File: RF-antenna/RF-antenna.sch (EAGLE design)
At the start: 7 parts, among them X1 SMA-V, X2 SMA-V, X3 SMA-V, X4 SMA-V, X5 SMA-V, X6 SMA-V

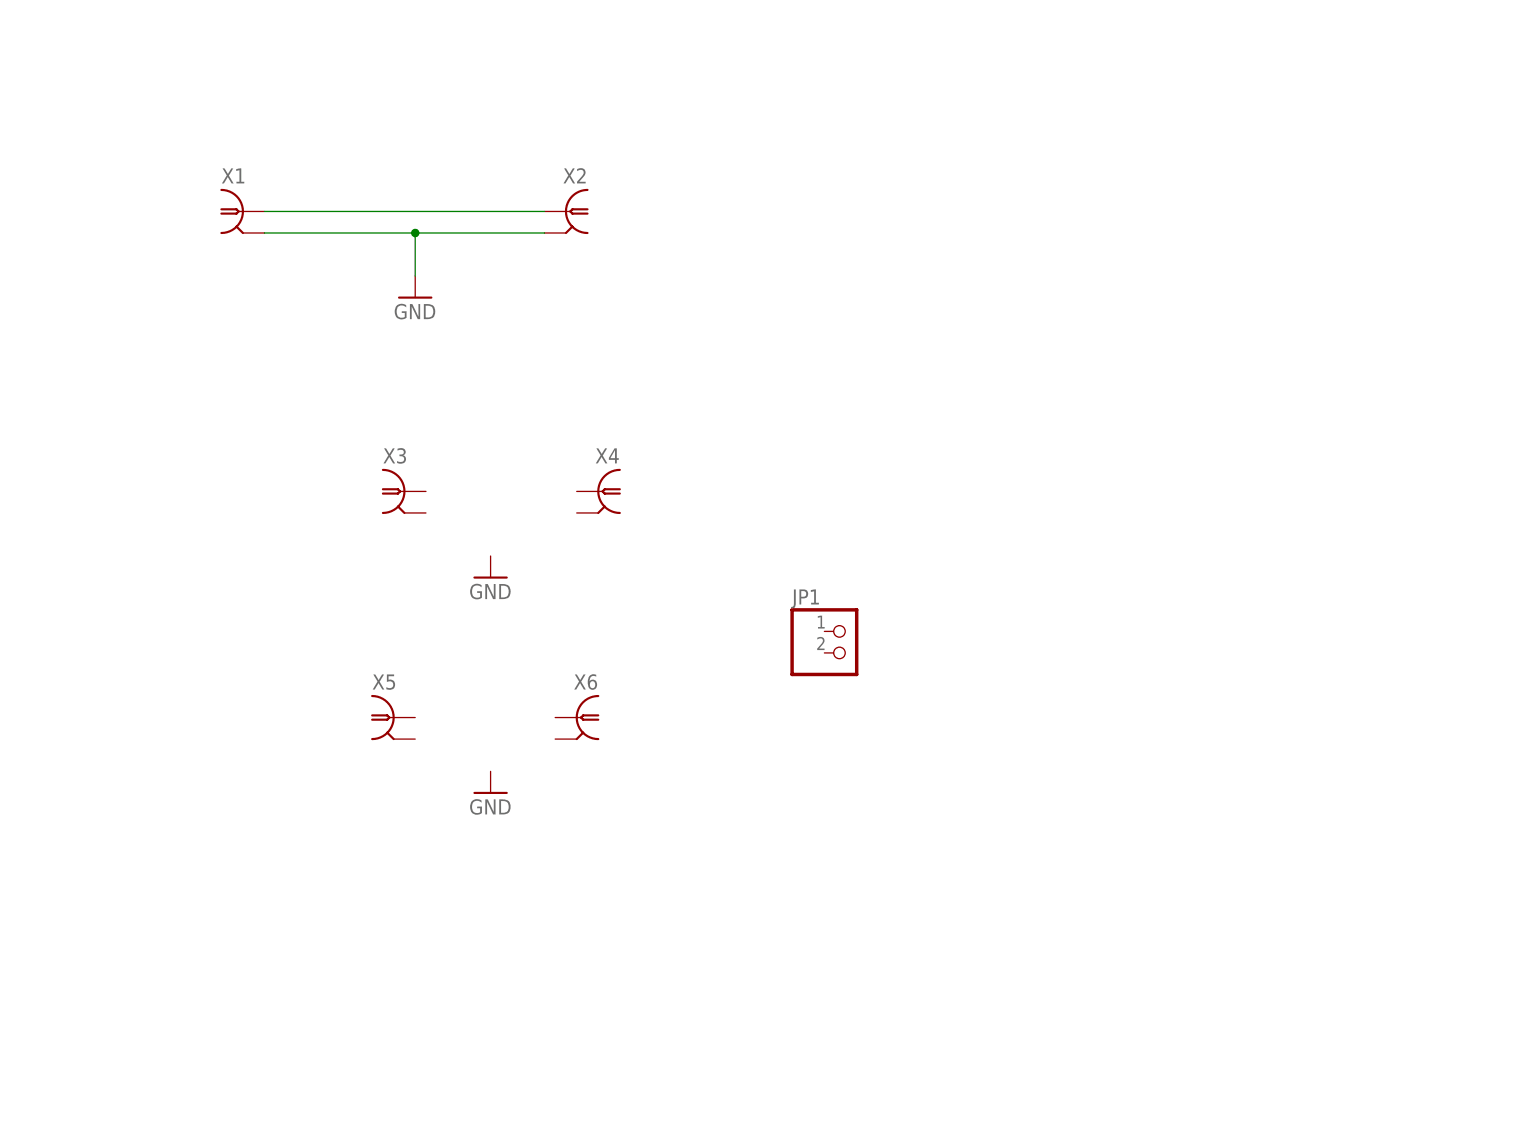
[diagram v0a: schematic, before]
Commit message: Adding parts for footprinting
Added a bunch of test components to get an idea of how tight the design
will be. Also corrected the keepout areas.

DSB
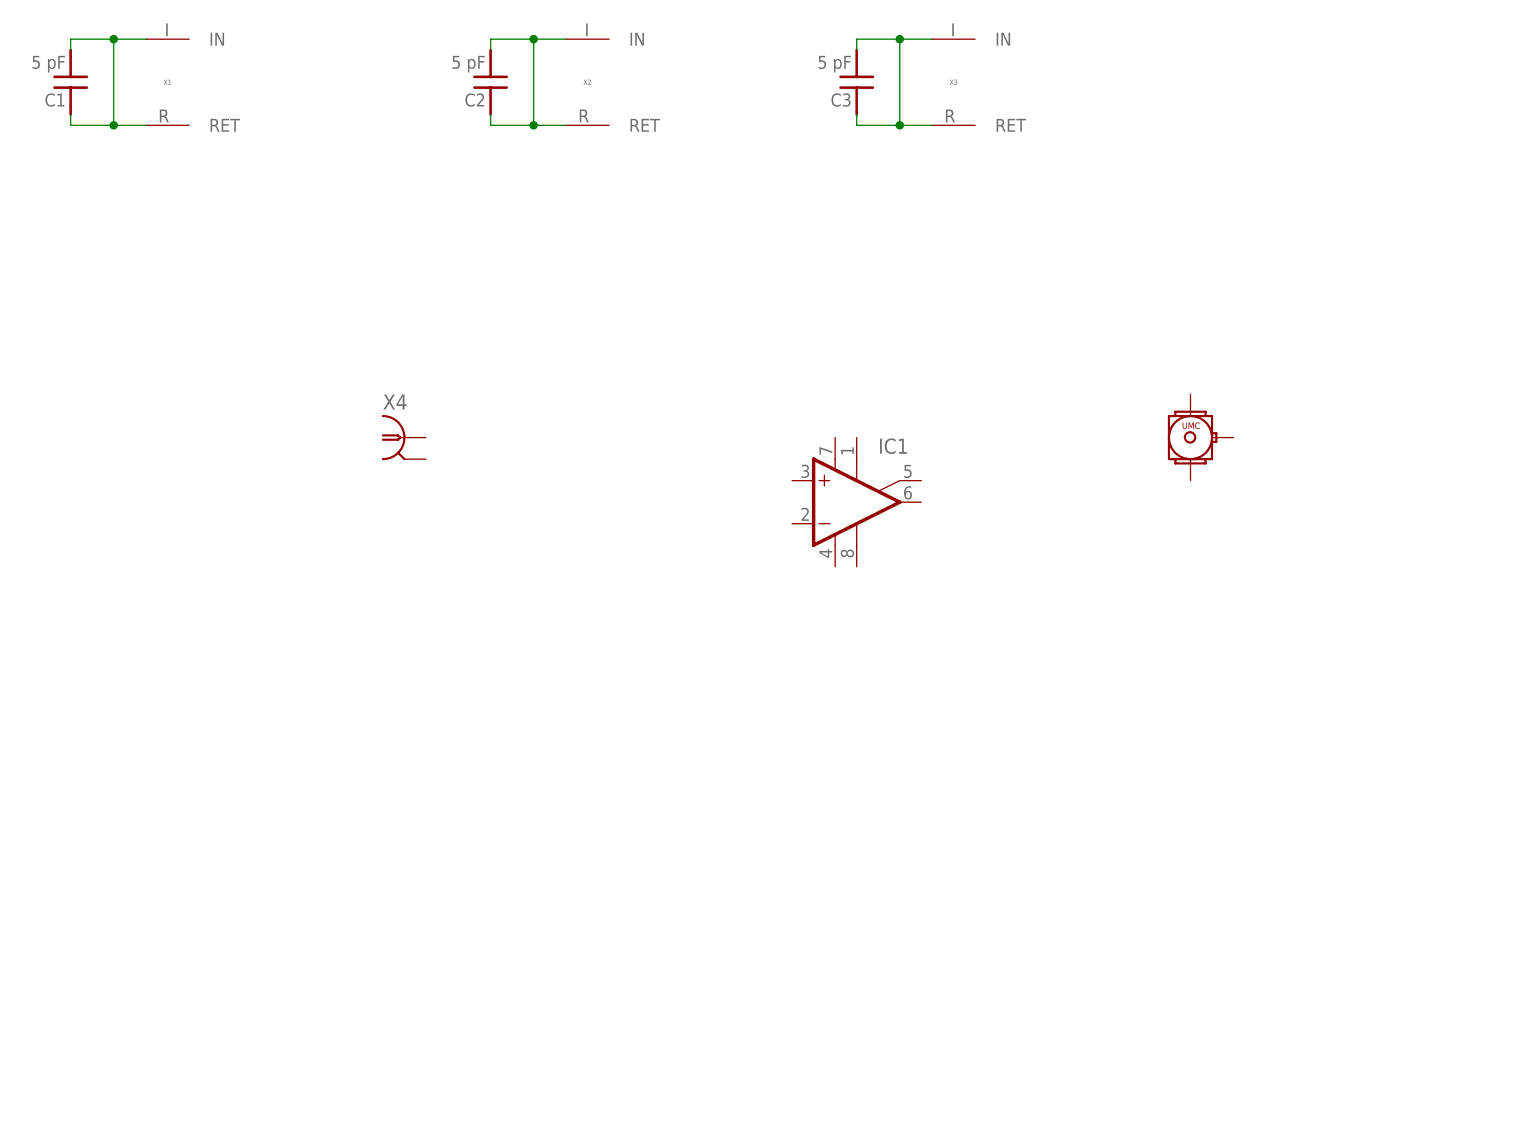
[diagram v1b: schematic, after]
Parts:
- removed JP1: (no value), pinhead:PINHD-1X2
- removed X5, X6: SMA-V, connector-jqi:SMA-V
- added C1, C2, C3: 5 pF, jqi_passives:C_MLCC_SMDCMLCC_0603
- added CON1: UMC_CONNECTORREGULAR, qkdlab_alessandro:UMC_CONNECTORREGULAR
- added IC1: (no value), opamp-jqi:OPAMP-SO
- X1, X2, X3: value SMA-V -> LG_HEADER; device connector-jqi:SMA-V -> connector-jqi:LG_HEADER
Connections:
- removed net GND: X1.2, X2.2
- new net N$2: C2.1, C2.2, X2.IN, X2.RET
- new net N$3: C3.1, C3.2, X3.IN, X3.RET
- net N$1: now also C1.1, C1.2, X1.IN, X1.RET; no longer X1.1, X2.1
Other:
- note added: "D Coil 1"
- note added: "D Coil 2"
- note added: "Round Coil"
- moved on the sheet: X4
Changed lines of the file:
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@@
 <?xml version="1.0" encoding="utf-8"?>
 <!DOCTYPE eagle SYSTEM "eagle.dtd">
-<eagle version="7.7.0">
+<eagle version="8.5.0">
 <drawing>
 <settings>
 <setting alwaysvectorfont="no"/>
+<setting keepoldvectorfont="yes"/>
 <setting verticaltext="up"/>
 </settings>
@@
 <parts>
 <part name="FRAME1" library="frames" deviceset="FRAME_A_L" device=""/>
-<part name="X1" library="connector-jqi" deviceset="SMA" device="-V"/>
-<part name="X2" library="connector-jqi" deviceset="SMA" device="-V"/>
-<part name="X3" library="connector-jqi" deviceset="SMA" device="-V"/>
+<part name="X1" library="connector-jqi" deviceset="LG_HEADER" device=""/>
+<part name="X2" library="connector-jqi" deviceset="LG_HEADER" device=""/>
+<part name="X3" library="connector-jqi" deviceset="LG_HEADER" device=""/>
+<part name="C1" library="jqi_passives" deviceset="C_MLCC_SMD" device="CMLCC_0603" value="5 pF"/>
+<part name="C2" library="jqi_passives" deviceset="C_MLCC_SMD" device="CMLCC_0603" value="5 pF"/>
+<part name="C3" library="jqi_passives" deviceset="C_MLCC_SMD" device="CMLCC_0603" value="5 pF"/>
 <part name="X4" library="connector-jqi" deviceset="SMA" device="-V"/>
-<part name="X5" library="connector-jqi" deviceset="SMA" device="-V"/>
-<part name="X6" library="connector-jqi" deviceset="SMA" device="-V"/>
-<part name="GND1" library="supply1" deviceset="GND" device=""/>
-<part name="GND2" library="supply1" deviceset="GND" device=""/>
-<part name="GND3" library="supply1" deviceset="GND" device=""/>
-<part name="JP1" library="pinhead" deviceset="PINHD-1X2" device=""/>
+<part name="IC1" library="opamp-jqi" deviceset="OPAMP" device="-SO"/>
+<part name="CON1" library="qkdlab_alessandro" deviceset="UMC_CONNECTOR" device="REGULAR"/>
 </parts>
 <sheets>
 <sheet>
 <plain>
+<text x="26.67" y="191.77" size="1.778" layer="98">Round Coil</text>
+<text x="77.47" y="191.77" size="1.778" layer="98">D Coil 1</text>
+<text x="120.65" y="191.77" size="1.778" layer="98">D Coil 2</text>
 </plain>
 <instances>
 <instance part="FRAME1" gate="G$1" x="0" y="0"/>
 <instance part="FRAME1" gate="G$2" x="172.72" y="0"/>
-<instance part="X1" gate="G$1" x="45.72" y="167.64"/>
-<instance part="X2" gate="G$1" x="83.82" y="167.64" rot="MR0"/>
-<instance part="X3" gate="G$1" x="64.77" y="134.62"/>
-<instance part="X4" gate="G$1" x="87.63" y="134.62" rot="MR0"/>
-<instance part="X5" gate="G$1" x="63.5" y="107.95"/>
-<instance part="X6" gate="G$1" x="85.09" y="107.95" rot="MR0"/>
-<instance part="GND1" gate="1" x="74.93" y="124.46"/>
-<instance part="GND2" gate="1" x="66.04" y="157.48"/>
-<instance part="GND3" gate="1" x="74.93" y="99.06"/>
-<instance part="JP1" gate="G$1" x="116.84" y="115.57"/>
+<instance part="X1" gate="G$1" x="39.37" y="182.88"/>
+<instance part="X2" gate="G$1" x="88.9" y="182.88"/>
+<instance part="X3" gate="G$1" x="132.08" y="182.88"/>
+<instance part="C1" gate="G$1" x="25.4" y="181.61" rot="R180"/>
+<instance part="C2" gate="G$1" x="74.93" y="181.61" rot="R180"/>
+<instance part="C3" gate="G$1" x="118.11" y="181.61" rot="R180"/>
+<instance part="X4" gate="G$1" x="64.77" y="140.97"/>
+<instance part="IC1" gate="G$1" x="115.57" y="133.35"/>
+<instance part="CON1" gate="G$1" x="157.48" y="140.97"/>
 </instances>
 <busses>
@@
 <net name="N$1" class="0">
 <segment>
-<pinref part="X1" gate="G$1" pin="1"/>
-<pinref part="X2" gate="G$1" pin="1"/>
-<wire x1="48.26" y1="167.64" x2="81.28" y2="167.64" width="0.1524" layer="91"/>
+<pinref part="X1" gate="G$1" pin="IN"/>
+<wire x1="34.29" y1="187.96" x2="30.48" y2="187.96" width="0.1524" layer="91"/>
+<wire x1="30.48" y1="187.96" x2="30.48" y2="177.8" width="0.1524" layer="91"/>
+<pinref part="X1" gate="G$1" pin="RET"/>
+<wire x1="30.48" y1="177.8" x2="34.29" y2="177.8" width="0.1524" layer="91"/>
+<pinref part="C1" gate="G$1" pin="2"/>
+<wire x1="30.48" y1="187.96" x2="25.4" y2="187.96" width="0.1524" layer="91"/>
+<wire x1="25.4" y1="187.96" x2="25.4" y2="186.69" width="0.1524" layer="91"/>
+<junction x="30.48" y="187.96"/>
+<pinref part="C1" gate="G$1" pin="1"/>
+<wire x1="25.4" y1="179.07" x2="25.4" y2="177.8" width="0.1524" layer="91"/>
+<wire x1="25.4" y1="177.8" x2="30.48" y2="177.8" width="0.1524" layer="91"/>
+<junction x="30.48" y="177.8"/>
 </segment>
 </net>
-<net name="GND" class="0">
+<net name="N$2" class="0">
 <segment>
-<pinref part="X1" gate="G$1" pin="2"/>
-<pinref part="X2" gate="G$1" pin="2"/>
-<wire x1="48.26" y1="165.1" x2="66.04" y2="165.1" width="0.1524" layer="91"/>
-<pinref part="GND2" gate="1" pin="GND"/>
-<wire x1="66.04" y1="165.1" x2="81.28" y2="165.1" width="0.1524" layer="91"/>
-<wire x1="66.04" y1="165.1" x2="66.04" y2="160.02" width="0.1524" layer="91"/>
-<junction x="66.04" y="165.1"/>
+<pinref part="X2" gate="G$1" pin="IN"/>
+<wire x1="83.82" y1="187.96" x2="80.01" y2="187.96" width="0.1524" layer="91"/>
+<wire x1="80.01" y1="187.96" x2="80.01" y2="177.8" width="0.1524" layer="91"/>
+<pinref part="X2" gate="G$1" pin="RET"/>
+<wire x1="80.01" y1="177.8" x2="83.82" y2="177.8" width="0.1524" layer="91"/>
+<pinref part="C2" gate="G$1" pin="2"/>
+<wire x1="80.01" y1="187.96" x2="74.93" y2="187.96" width="0.1524" layer="91"/>
+<wire x1="74.93" y1="187.96" x2="74.93" y2="186.69" width="0.1524" layer="91"/>
+<junction x="80.01" y="187.96"/>
+<pinref part="C2" gate="G$1" pin="1"/>
+<wire x1="74.93" y1="179.07" x2="74.93" y2="177.8" width="0.1524" layer="91"/>
+<wire x1="74.93" y1="177.8" x2="80.01" y2="177.8" width="0.1524" layer="91"/>
+<junction x="80.01" y="177.8"/>
 </segment>
 </net>
+<net name="N$3" class="0">
+<segment>
+<pinref part="X3" gate="G$1" pin="IN"/>
+<wire x1="127" y1="187.96" x2="123.19" y2="187.96" width="0.1524" layer="91"/>
+<wire x1="123.19" y1="187.96" x2="123.19" y2="177.8" width="0.1524" layer="91"/>
+<pinref part="X3" gate="G$1" pin="RET"/>
+<wire x1="123.19" y1="177.8" x2="127" y2="177.8" width="0.1524" layer="91"/>
+<pinref part="C3" gate="G$1" pin="2"/>
+<wire x1="123.19" y1="187.96" x2="118.11" y2="187.96" width="0.1524" layer="91"/>
+<wire x1="118.11" y1="187.96" x2="118.11" y2="186.69" width="0.1524" layer="91"/>
+<junction x="123.19" y="187.96"/>
+<pinref part="C3" gate="G$1" pin="1"/>
+<wire x1="118.11" y1="179.07" x2="118.11" y2="177.8" width="0.1524" layer="91"/>
+<wire x1="118.11" y1="177.8" x2="123.19" y2="177.8" width="0.1524" layer="91"/>
+<junction x="123.19" y="177.8"/>
+</segment>
+</net>

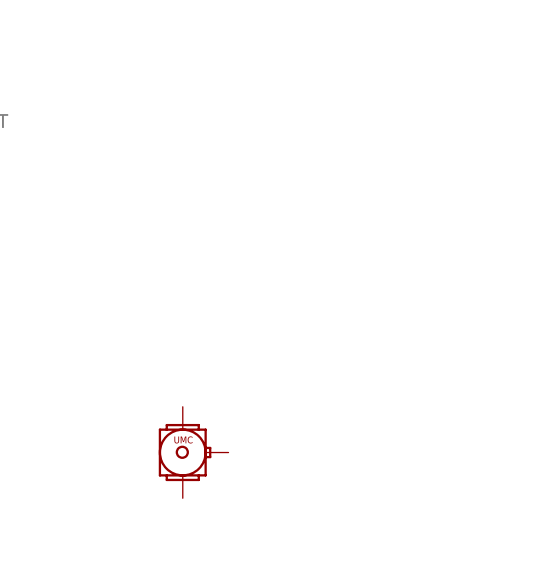
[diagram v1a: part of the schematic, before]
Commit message: More footprints
Added a few more component footprints to see what is up and test layout.

DSB
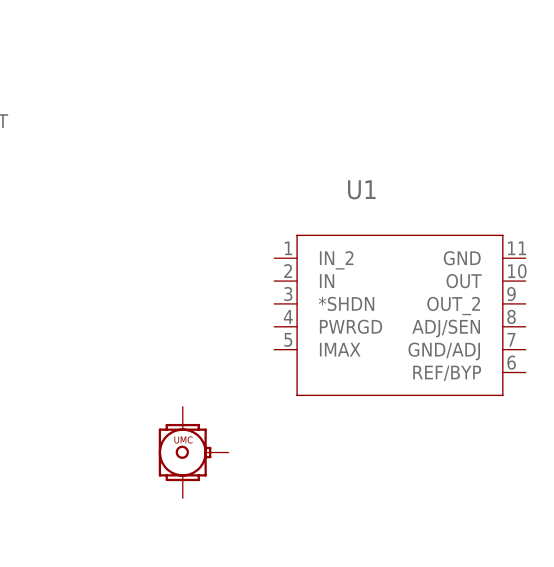
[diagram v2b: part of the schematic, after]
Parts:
- added U1: (no value), linear-technology-jqi:LT3065EDDPBF
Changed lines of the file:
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@@
 <?xml version="1.0" encoding="utf-8"?>
 <!DOCTYPE eagle SYSTEM "eagle.dtd">
-<eagle version="8.5.0">
+<eagle version="7.7.0">
 <drawing>
 <settings>
 <setting alwaysvectorfont="no"/>
-<setting keepoldvectorfont="yes"/>
 <setting verticaltext="up"/>
 </settings>
@@
 <part name="IC1" library="opamp-jqi" deviceset="OPAMP" device="-SO"/>
 <part name="CON1" library="qkdlab_alessandro" deviceset="UMC_CONNECTOR" device="REGULAR"/>
+<part name="U1" library="linear-technology-jqi" deviceset="LT3065EDDPBF" device=""/>
 </parts>
 <sheets>
@@
 <instance part="IC1" gate="G$1" x="115.57" y="133.35"/>
 <instance part="CON1" gate="G$1" x="157.48" y="140.97"/>
+<instance part="U1" gate="A" x="180.34" y="154.94"/>
 </instances>
 <busses>
